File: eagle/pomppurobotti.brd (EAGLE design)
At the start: 100 x 80 mm, 3 parts

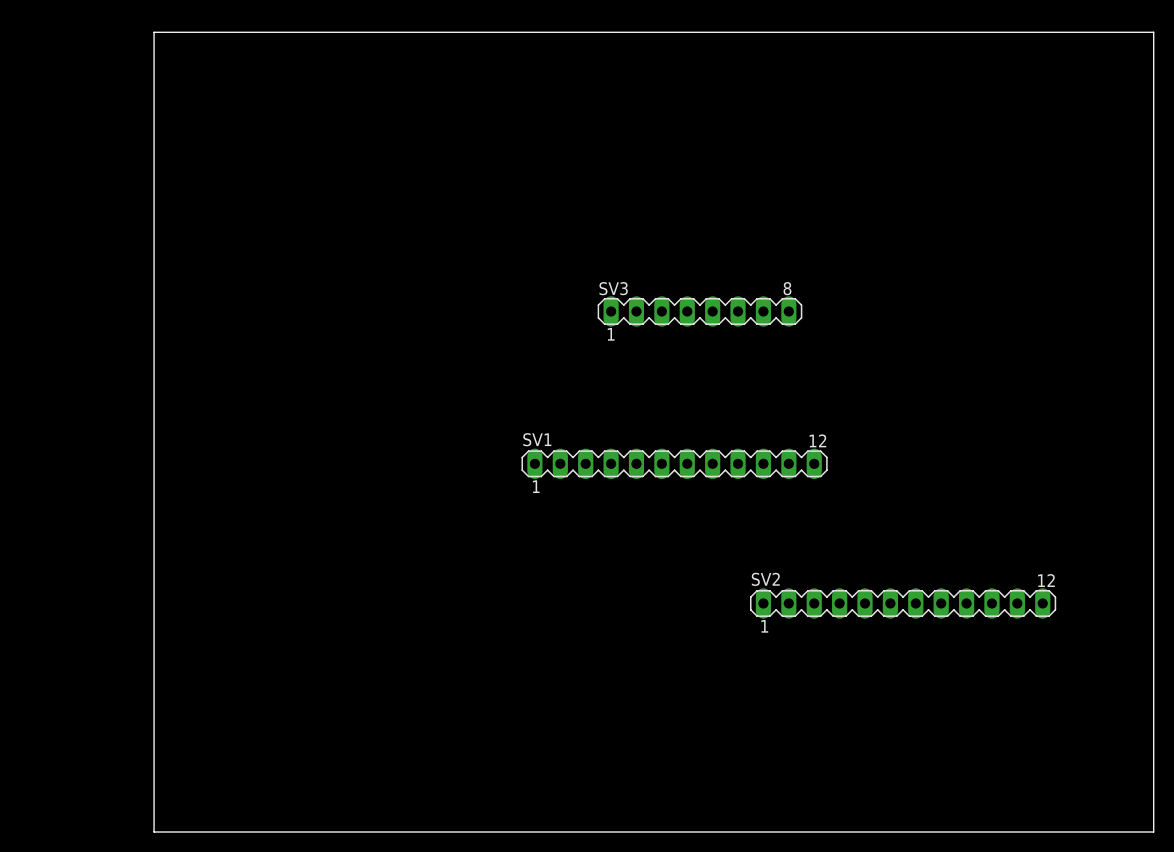
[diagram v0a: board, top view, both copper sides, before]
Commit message: Updates to schemantic and board files
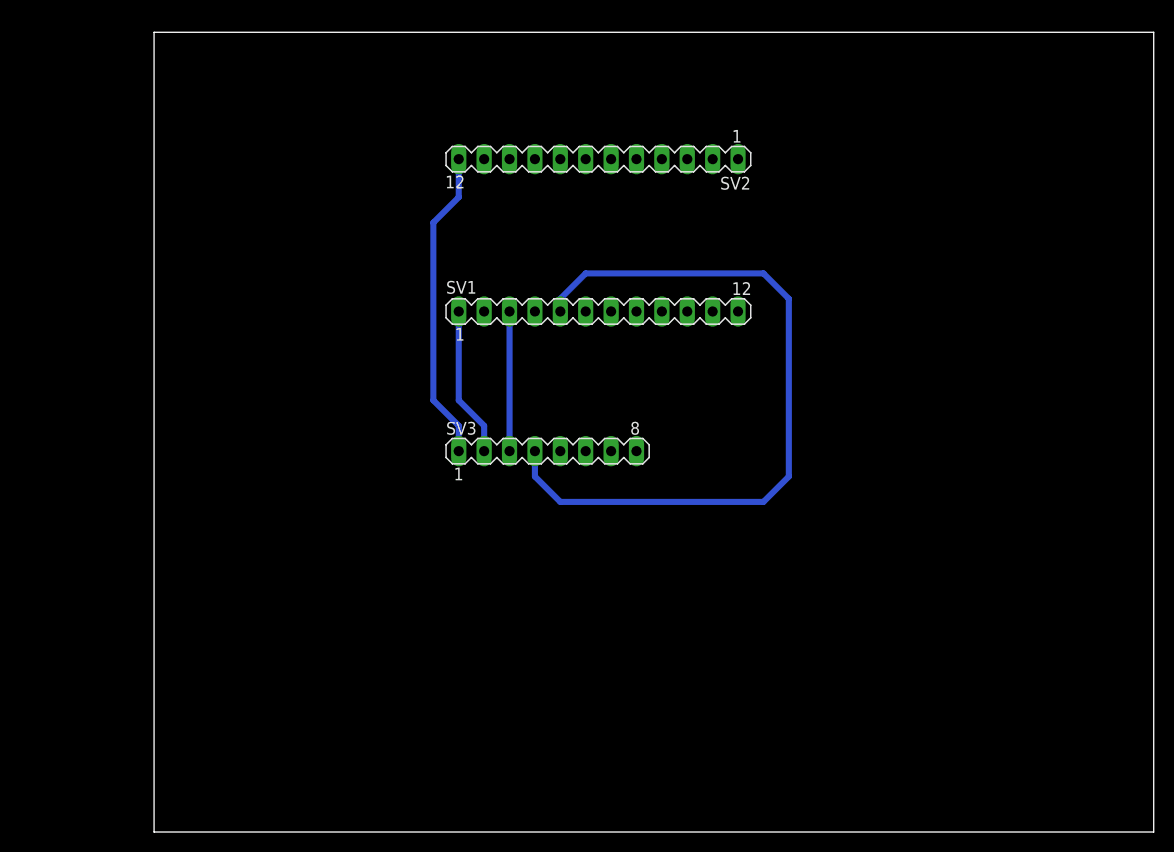
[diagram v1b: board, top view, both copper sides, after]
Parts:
- moved SV2 53.9 mm to (44.5, 67.3), turned to 180 degrees
- moved SV3 20.7 mm to (39.4, 38.1)
- moved SV1 17.0 mm to (44.5, 52.1)
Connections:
- net MOSI: now also SV1.4
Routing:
- net MISO: track 0.00 -> 74.1 mm
- net +5V: track 0.00 -> 31.3 mm
- net GND: track 0.00 -> 15.0 mm
- net SCLK: track 0.00 -> 14.0 mm
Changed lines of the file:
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@@
 <setting verticaltext="up"/>
 </settings>
-<grid distance="0.05" unitdist="inch" unit="inch" style="lines" multiple="1" display="no" altdistance="0.025" altunitdist="inch" altunit="inch"/>
+<grid distance="0.1" unitdist="inch" unit="inch" style="lines" multiple="1" display="yes" altdistance="0.025" altunitdist="inch" altunit="inch"/>
 <layers>
 <layer number="1" name="Top" color="4" fill="1" visible="yes" active="yes"/>
@@
 </class>
 </classes>
-<designrules name="default">
+<designrules name="default *">
 <description language="de">&lt;b&gt;EAGLE Design Rules&lt;/b&gt;
 &lt;p&gt;
@@
 <param name="mtCopper" value="0.035mm 0.035mm 0.035mm 0.035mm 0.035mm 0.035mm 0.035mm 0.035mm 0.035mm 0.035mm 0.035mm 0.035mm 0.035mm 0.035mm 0.035mm 0.035mm"/>
 <param name="mtIsolate" value="1.5mm 0.15mm 0.2mm 0.15mm 0.2mm 0.15mm 0.2mm 0.15mm 0.2mm 0.15mm 0.2mm 0.15mm 0.2mm 0.15mm 0.2mm"/>
-<param name="mdWireWire" value="8mil"/>
-<param name="mdWirePad" value="8mil"/>
-<param name="mdWireVia" value="8mil"/>
-<param name="mdPadPad" value="8mil"/>
-<param name="mdPadVia" value="8mil"/>
-<param name="mdViaVia" value="8mil"/>
+<param name="mdWireWire" value="10mil"/>
+<param name="mdWirePad" value="10mil"/>
+<param name="mdWireVia" value="10mil"/>
+<param name="mdPadPad" value="10mil"/>
+<param name="mdPadVia" value="10mil"/>
+<param name="mdViaVia" value="10mil"/>
 <param name="mdSmdPad" value="8mil"/>
 <param name="mdSmdVia" value="8mil"/>
@@
 </autorouter>
 <elements>
-<element name="SV1" library="con-lstb" package="MA12-1" value="" x="52.07" y="36.83">
-<attribute name="OC_NEWARK" value="unknown" x="52.07" y="36.83" size="1.778" layer="27" display="off"/>
-<attribute name="MPN" value="" x="52.07" y="36.83" size="1.778" layer="27" display="off"/>
-<attribute name="MF" value="" x="52.07" y="36.83" size="1.778" layer="27" display="off"/>
-<attribute name="OC_FARNELL" value="unknown" x="52.07" y="36.83" size="1.778" layer="27" display="off"/>
+<element name="SV1" library="con-lstb" package="MA12-1" value="" x="44.45" y="52.07">
+<attribute name="OC_NEWARK" value="unknown" x="44.45" y="52.07" size="1.778" layer="27" display="off"/>
+<attribute name="MPN" value="" x="44.45" y="52.07" size="1.778" layer="27" display="off"/>
+<attribute name="MF" value="" x="44.45" y="52.07" size="1.778" layer="27" display="off"/>
+<attribute name="OC_FARNELL" value="unknown" x="44.45" y="52.07" size="1.778" layer="27" display="off"/>
 </element>
-<element name="SV2" library="con-lstb" package="MA12-1" value="" x="74.93" y="22.86">
-<attribute name="OC_NEWARK" value="unknown" x="74.93" y="22.86" size="1.778" layer="27" display="off"/>
-<attribute name="MPN" value="" x="74.93" y="22.86" size="1.778" layer="27" display="off"/>
-<attribute name="MF" value="" x="74.93" y="22.86" size="1.778" layer="27" display="off"/>
-<attribute name="OC_FARNELL" value="unknown" x="74.93" y="22.86" size="1.778" layer="27" display="off"/>
+<element name="SV2" library="con-lstb" package="MA12-1" value="" x="44.45" y="67.31" rot="R180">
+<attribute name="OC_NEWARK" value="unknown" x="44.45" y="67.31" size="1.778" layer="27" rot="R180" display="off"/>
+<attribute name="MPN" value="" x="44.45" y="67.31" size="1.778" layer="27" rot="R180" display="off"/>
+<attribute name="MF" value="" x="44.45" y="67.31" size="1.778" layer="27" rot="R180" display="off"/>
+<attribute name="OC_FARNELL" value="unknown" x="44.45" y="67.31" size="1.778" layer="27" rot="R180" display="off"/>
 </element>
-<element name="SV3" library="con-lstb" package="MA08-1" value="" x="54.61" y="52.07">
-<attribute name="OC_NEWARK" value="unknown" x="54.61" y="52.07" size="1.778" layer="27" display="off"/>
-<attribute name="MPN" value="" x="54.61" y="52.07" size="1.778" layer="27" display="off"/>
-<attribute name="MF" value="" x="54.61" y="52.07" size="1.778" layer="27" display="off"/>
-<attribute name="OC_FARNELL" value="unknown" x="54.61" y="52.07" size="1.778" layer="27" display="off"/>
+<element name="SV3" library="con-lstb" package="MA08-1" value="" x="39.37" y="38.1">
+<attribute name="OC_NEWARK" value="unknown" x="39.37" y="38.1" size="1.778" layer="27" display="off"/>
+<attribute name="MPN" value="" x="39.37" y="38.1" size="1.778" layer="27" display="off"/>
+<attribute name="MF" value="" x="39.37" y="38.1" size="1.778" layer="27" display="off"/>
+<attribute name="OC_FARNELL" value="unknown" x="39.37" y="38.1" size="1.778" layer="27" display="off"/>
 </element>
 </elements>
@@
 <contactref element="SV3" pad="2"/>
 <contactref element="SV1" pad="1"/>
-<wire x1="38.1" y1="36.83" x2="48.26" y2="52.07" width="0" layer="19" extent="1-1"/>
+<wire x1="30.48" y1="52.07" x2="30.48" y2="43.18" width="0.6096" layer="16"/>
+<wire x1="30.48" y1="43.18" x2="33.02" y2="40.64" width="0.6096" layer="16"/>
+<wire x1="33.02" y1="40.64" x2="33.02" y2="38.1" width="0.6096" layer="16"/>
 </signal>
 <signal name="0">
@@
 <contactref element="SV1" pad="3"/>
 <contactref element="SV3" pad="3"/>
-<wire x1="43.18" y1="36.83" x2="50.8" y2="52.07" width="0" layer="19" extent="1-1"/>
+<wire x1="35.56" y1="52.07" x2="35.56" y2="38.1" width="0.6096" layer="16"/>
 </signal>
 <signal name="MISO">
 <contactref element="SV3" pad="4"/>
 <contactref element="SV1" pad="5"/>
-<wire x1="48.26" y1="36.83" x2="53.34" y2="52.07" width="0" layer="19" extent="1-1"/>
+<wire x1="40.64" y1="52.07" x2="40.64" y2="53.34" width="0.6096" layer="16"/>
+<wire x1="40.64" y1="53.34" x2="43.18" y2="55.88" width="0.6096" layer="16"/>
+<wire x1="43.18" y1="55.88" x2="60.96" y2="55.88" width="0.6096" layer="16"/>
+<wire x1="60.96" y1="55.88" x2="63.5" y2="53.34" width="0.6096" layer="16"/>
+<wire x1="63.5" y1="53.34" x2="63.5" y2="35.56" width="0.6096" layer="16"/>
+<wire x1="38.1" y1="38.1" x2="38.1" y2="35.56" width="0.6096" layer="16"/>
+<wire x1="38.1" y1="35.56" x2="40.64" y2="33.02" width="0.6096" layer="16"/>
+<wire x1="40.64" y1="33.02" x2="60.96" y2="33.02" width="0.6096" layer="16"/>
+<wire x1="60.96" y1="33.02" x2="63.5" y2="35.56" width="0.6096" layer="16"/>
 </signal>
 <signal name="+3.3V">
@@
 <contactref element="SV2" pad="12"/>
 <contactref element="SV3" pad="1"/>
-<wire x1="45.72" y1="52.07" x2="88.9" y2="22.86" width="0" layer="19" extent="1-1"/>
+<wire x1="30.48" y1="67.31" x2="30.48" y2="63.5" width="0.6096" layer="16"/>
+<wire x1="30.48" y1="63.5" x2="27.94" y2="60.96" width="0.6096" layer="16"/>
+<wire x1="27.94" y1="60.96" x2="27.94" y2="43.18" width="0.6096" layer="16"/>
+<wire x1="27.94" y1="43.18" x2="30.48" y2="40.64" width="0.6096" layer="16"/>
+<wire x1="30.48" y1="40.64" x2="30.48" y2="38.1" width="0.6096" layer="16"/>
 </signal>
 <signal name="N$14">
@@
 <signal name="MOSI">
 <contactref element="SV3" pad="5"/>
+<contactref element="SV1" pad="4"/>
+<wire x1="40.64" y1="38.1" x2="38.1" y2="52.07" width="0" layer="19" extent="1-1"/>
 </signal>
 </signals>

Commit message: First version of PCB
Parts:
- removed SV1, SV2: (no value), con-lstb:MA12-1
- removed SV3: (no value), con-lstb:MA08-1
- added ACCELOM: (no value), SparkFun-Connectors:1X06
- added C1, C2: 10uF, SparkFun-Capacitors:CAP-PTH-SMALL
- added EXTRA: (no value), SparkFun-Connectors:1X03
- added IC1: (no value), SparkFun-PowerIC:TO-220-ALT
- added JP1: POWER_JACK1, SparkFun-Connectors:POWER_JACK_SMD_OVERPASTE_REDBOARD_0603
- added LED1, LED2: RED, SparkFun-LED:LED5MM
- added MORORD_R, MOTORD_L: (no value), SparkFun-Connectors:1X08_LONGPADS
- added MOTORS: (no value), SparkFun-Connectors:1X04
- added PIEZO: EFBAA40D101, buzzer:EFBAA40D101
- added Q1: MOSFET-NCHANNELFQP30N06L, SparkFun-DiscreteSemi:TO220V
- added R1, R2: 220Ω, SparkFun-Resistors:AXIAL-0.3
- added RADIO: (no value), SparkFun-Connectors:1X08_ROUND
- added RANGEF: (no value), SparkFun-Connectors:1X05
- added RV1: (no value), SparkFun-Electromechanical:TRIM_POT
- added S1: SWITCH-MOMENTARY-2PTH, SparkFun-Electromechanical:TACTILE-PTH
- added SPRING_PINS: M02PTH, SparkFun-Connectors:1X02
- added TEENSY_1, TEENSY_2: M12PTH, SparkFun-Connectors:1X12
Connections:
- removed net +5V: SV2.12, SV3.1
- removed net 0: SV1.2
- removed net 10: SV1.12
- removed net 4: SV1.6
- removed net 5: SV1.7
- removed net 6: SV1.8
- removed net 7: SV1.9
- removed net 8: SV1.10
- removed net 9: SV1.11
- removed net N$14: SV2.11
- removed net N$15: SV2.10
- removed net N$16: SV2.9
- removed net N$17: SV2.8
- removed net N$18: SV2.7
- removed net N$19: SV2.6
- removed net N$20: SV2.5
- removed net N$21: SV2.4
- removed net N$22: SV2.3
- removed net N$23: SV2.2
- removed net N$24: SV2.1
- new net A0: ACCELOM.2, TEENSY_2.9
- new net A01: MOTORD_L.4, MOTORS.4
- new net A02: MOTORD_L.5, MOTORS.3
- new net A1: ACCELOM.3, TEENSY_2.10
- new net A2: ACCELOM.4, TEENSY_2.11
- new net A4: EXTRA.1, TEENSY_2.7
- new net A5: EXTRA.2, TEENSY_2.6
- new net A8: RV1.1, TEENSY_2.3
- new net AIN1: MORORD_R.6, TEENSY_1.8
- new net AIN2: MORORD_R.7, TEENSY_1.2
- new net AN: RANGEF.1, TEENSY_2.8
- new net B01: MOTORD_L.7, MOTORS.1
- new net B02: MOTORD_L.6, MOTORS.2
- new net BIN1: MORORD_R.4, TEENSY_1.9
- new net BIN2: MORORD_R.3, TEENSY_1.10
- new net LEDA10: R2.P$1, TEENSY_2.1
- new net N$2: LED1.K, R1.P$2
- new net N$3: C1.1, IC1.IN, JP1.VIN0
- new net N$4: LED2.A, R2.P$2
- new net N$5: Q1.2, SPRING_PINS.2
- new net PWMA: MORORD_R.8, TEENSY_1.12, TEENSY_1.6
- new net PWMA6: EXTRA.3, TEENSY_2.5
- new net PWMA7: PIEZO.2, TEENSY_2.4
- new net PWMA9: S1.1, TEENSY_2.2
- new net PWMB: MORORD_R.2, TEENSY_1.11
- new net PWMC: Q1.1, TEENSY_1.7
- new net VCC: ACCELOM.6, C2.1, IC1.OUT, LED1.A, MORORD_R.5, MOTORD_L.1, MOTORD_L.2, Q1.3, RADIO.1, RANGEF.4, RV1.3, S1.3, TEENSY_2.12
- net +3.3V: now also RADIO.8; no longer SV3.8
- net GND: now also ACCELOM.5, C1.2, C2.2, IC1.GND, JP1.P$4, LED2.K, MORORD_R.1, MOTORD_L.3, MOTORD_L.8, PIEZO.1, R1.P$1, RADIO.2, RANGEF.5, RV1.2, SPRING_PINS.1, TEENSY_1.1; no longer SV1.1, SV3.2
- net IRQ: now also RADIO.7; no longer SV3.7
- net MISO: now also RADIO.4, TEENSY_1.5; no longer SV1.5, SV3.4
- net MOSI: now also RADIO.5, TEENSY_1.4; no longer SV1.4, SV3.5
- net SCLK: now also RADIO.3, TEENSY_1.3; no longer SV1.3, SV3.3
- net SEL: now also RADIO.6; no longer SV3.6
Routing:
- net VCC: track 0.00 -> 198.5 mm
- net PWMA: track 0.00 -> 32.4 mm
- net AIN2: track 0.00 -> 31.3 mm
- net +5V: track 31.3 -> 0.00 mm
- net A8: track 0.00 -> 30.3 mm
- net MISO: track 74.1 -> 43.9 mm
- net MOSI: track 0.00 -> 29.8 mm
- net PWMC: track 0.00 -> 27.9 mm, vias 0 -> 2
- net AN: track 0.00 -> 21.5 mm
- net PWMA9: track 0.00 -> 19.3 mm
- net SCLK: track 14.0 -> 29.8 mm
- net PWMA7: track 0.00 -> 14.2 mm
- net PWMB: track 0.00 -> 13.8 mm
- net BIN2: track 0.00 -> 13.8 mm
- net BIN1: track 0.00 -> 13.8 mm
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- added copper zone on layer 1, net GND
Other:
- board size 100 x 80 mm -> 71.4 x 70.5 mm

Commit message: Many major improvements
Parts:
- added POWER_INPUT_2: M02PTH, SparkFun-Connectors:1X02
- JP1: value POWER_JACK1 -> POWER_JACKPTH; device SparkFun-Connectors:POWER_JACK_SMD_OVERPASTE_REDBOARD_0603 -> SparkFun-Connectors:POWER_JACK_PTH
- moved PIEZO 75.0 mm to (10.6, 14.0), turned to 0 degrees
- moved SPRING_PINS 31.2 mm to (3.81, 29.2), turned to 270 degrees
- moved LED2 11.4 mm to (59.7, 73.0), turned to 90 degrees
- moved ACCELOM 10.8 mm to (55.9, 49.5)
- moved EXTRA 9.67 mm to (55.9, 53.3)
- moved JP1 8.91 mm to (-2.54, 60.3), turned to 270 degrees
- moved Q1 7.73 mm to (26.7, 21.6)
- moved TEENSY_2 7.62 mm to (48.3, 59.7)
- moved TEENSY_1 7.62 mm to (33.0, 59.7)
- moved R2 6.63 mm to (57.8, 66.0), turned to 0 degrees
- moved RADIO 4.58 mm to (25.4, 69.8)
- moved S1 4.49 mm to (51.4, 73.0)
- moved IC1 4.49 mm to (5.71, 73.0)
- moved C1 3.18 mm to (11.4, 67.9), turned to 0 degrees
- moved MORORD_R 2.54 mm to (25.4, 29.2)
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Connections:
- net GND: now also JP1.GND, POWER_INPUT_2.1; no longer JP1.P$4
- net N$3: now also JP1.PWR, POWER_INPUT_2.2; no longer JP1.VIN0
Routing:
- net PWMA7: track 14.2 -> 109.1 mm
- net N$5: track 5.08 -> 26.6 mm
- net VCC: track 198.5 -> 211.2 mm
- net SCLK: track 29.8 -> 18.8 mm
- net N$3: track 8.16 -> 18.0 mm
- net MOSI: track 29.8 -> 21.8 mm
- net PWMA6: track 3.81 -> 11.7 mm
- net A5: track 3.81 -> 11.7 mm
- net A4: track 3.81 -> 11.7 mm
- net AIN2: track 31.3 -> 25.8 mm
- net BIN2: track 13.8 -> 8.22 mm
- net BIN1: track 13.8 -> 8.22 mm
- net AN: track 21.5 -> 26.7 mm
- net AIN1: track 12.7 -> 7.62 mm
- net A8: track 30.3 -> 35.3 mm
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- added copper zone on layer 16, net GND
- removed copper zone on layer 1, net GND
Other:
- board size 71.4 x 70.5 mm -> 66.3 x 70.5 mm

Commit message: Fix to proximity sensor position etc
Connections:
- new net PWMD: TEENSY_1.12
- net PWMA: no longer TEENSY_1.12
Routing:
- net PWMA: track 30.0 -> 7.62 mm
- net GND: track 9.52 -> 0.00 mm
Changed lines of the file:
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@@
 <layer number="16" name="Bottom" color="9" fill="1" visible="yes" active="yes"/>
 <layer number="17" name="Pads" color="2" fill="1" visible="yes" active="yes"/>
-<layer number="18" name="Vias" color="2" fill="1" visible="no" active="yes"/>
+<layer number="18" name="Vias" color="2" fill="1" visible="yes" active="yes"/>
 <layer number="19" name="Unrouted" color="6" fill="1" visible="yes" active="yes"/>
-<layer number="20" name="Dimension" color="15" fill="1" visible="no" active="yes"/>
-<layer number="21" name="tPlace" color="16" fill="1" visible="no" active="yes"/>
-<layer number="22" name="bPlace" color="14" fill="1" visible="no" active="yes"/>
-<layer number="23" name="tOrigins" color="15" fill="1" visible="no" active="yes"/>
-<layer number="24" name="bOrigins" color="15" fill="1" visible="no" active="yes"/>
-<layer number="25" name="tNames" color="7" fill="1" visible="no" active="yes"/>
-<layer number="26" name="bNames" color="7" fill="1" visible="no" active="yes"/>
-<layer number="27" name="tValues" color="7" fill="1" visible="no" active="yes"/>
-<layer number="28" name="bValues" color="7" fill="1" visible="no" active="yes"/>
+<layer number="20" name="Dimension" color="15" fill="1" visible="yes" active="yes"/>
+<layer number="21" name="tPlace" color="16" fill="1" visible="yes" active="yes"/>
+<layer number="22" name="bPlace" color="14" fill="1" visible="yes" active="yes"/>
+<layer number="23" name="tOrigins" color="15" fill="1" visible="yes" active="yes"/>
+<layer number="24" name="bOrigins" color="15" fill="1" visible="yes" active="yes"/>
+<layer number="25" name="tNames" color="7" fill="1" visible="yes" active="yes"/>
+<layer number="26" name="bNames" color="7" fill="1" visible="yes" active="yes"/>
+<layer number="27" name="tValues" color="7" fill="1" visible="yes" active="yes"/>
+<layer number="28" name="bValues" color="7" fill="1" visible="yes" active="yes"/>
 <layer number="29" name="tStop" color="7" fill="3" visible="no" active="yes"/>
 <layer number="30" name="bStop" color="7" fill="6" visible="no" active="yes"/>
@@
 <layer number="49" name="Reference" color="7" fill="1" visible="no" active="yes"/>
 <layer number="50" name="dxf" color="7" fill="1" visible="no" active="no"/>
-<layer number="51" name="tDocu" color="6" fill="1" visible="no" active="yes"/>
+<layer number="51" name="tDocu" color="6" fill="1" visible="yes" active="yes"/>
 <layer number="52" name="bDocu" color="7" fill="1" visible="no" active="yes"/>
 <layer number="53" name="tGND_GNDA" color="7" fill="9" visible="no" active="no"/>
@@
 <contactref element="PIEZO" pad="1"/>
 <contactref element="RANGEF" pad="5"/>
-<wire x1="19.05" y1="60.325" x2="28.575" y2="60.325" width="0.6096" layer="1"/>
+<wire x1="19.05" y1="60.325" x2="28.575" y2="60.325" width="0" layer="19" extent="1-16"/>
 <contactref element="RV1" pad="2"/>
 <contactref element="POWER_INPUT_2" pad="1"/>
@@
 <contactref element="MORORD_R" pad="8"/>
 <contactref element="TEENSY_1" pad="6"/>
-<contactref element="TEENSY_1" pad="12"/>
-<wire x1="38.1" y1="36.83" x2="33.02" y2="31.75" width="0.6096" layer="16"/>
-<wire x1="38.1" y1="46.99" x2="38.1" y2="36.83" width="0.6096" layer="16"/>
-<wire x1="33.02" y1="46.99" x2="38.1" y2="46.99" width="0.6096" layer="16"/>
 <wire x1="33.02" y1="46.99" x2="25.4" y2="46.99" width="0.6096" layer="16"/>
 </signal>
@@
 <signal name="N$1">
 </signal>
+<signal name="PWMD">
+<contactref element="TEENSY_1" pad="12"/>
+</signal>
 </signals>
